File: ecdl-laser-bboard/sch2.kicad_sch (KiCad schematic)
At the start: 0 parts

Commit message: slow bias DAC
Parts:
- added C38: 0.1u, Capacitor_SMD:C_0603_1608Metric, symbol Device:C
- added C39: 1u, Capacitor_SMD:C_0603_1608Metric, symbol Device:C
- added C40: 0.22u, Capacitor_SMD:C_0603_1608Metric, symbol Device:C
- added D5: D_Zener, symbol Device:D_Zener
- added IC1: DAC80501ZDGSR, SOP50P490X110-10N, symbol DAC80501ZDGSR:DAC80501ZDGSR
- added Q1: 2N7002, Package_TO_SOT_SMD:SOT-23, symbol Transistor_FET:2N7002
- added R28: 1k, Resistor_SMD:R_0603_1608Metric, symbol Device:R
- added R29: 100k, Resistor_SMD:R_0603_1608Metric, symbol Device:R
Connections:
- new net: D5.1 (K), Q1.1 (G), R28.2, R29.1
- new net +5V: C38.1, C39.1, IC1.1 (VDD)
- new net LDTC_COM: C38.2, C39.2, C40.2, D5.2 (A), IC1.4 (AGND), Q1.2 (S), R29.2
- new net LD_SHD: Q1.3 (D)
- new net RP_EN: R28.1
- new net V_REF: C40.1, IC1.10 (VREFIO)
- no-connect marks 0 -> 2
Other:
- note added: "LD Enable"

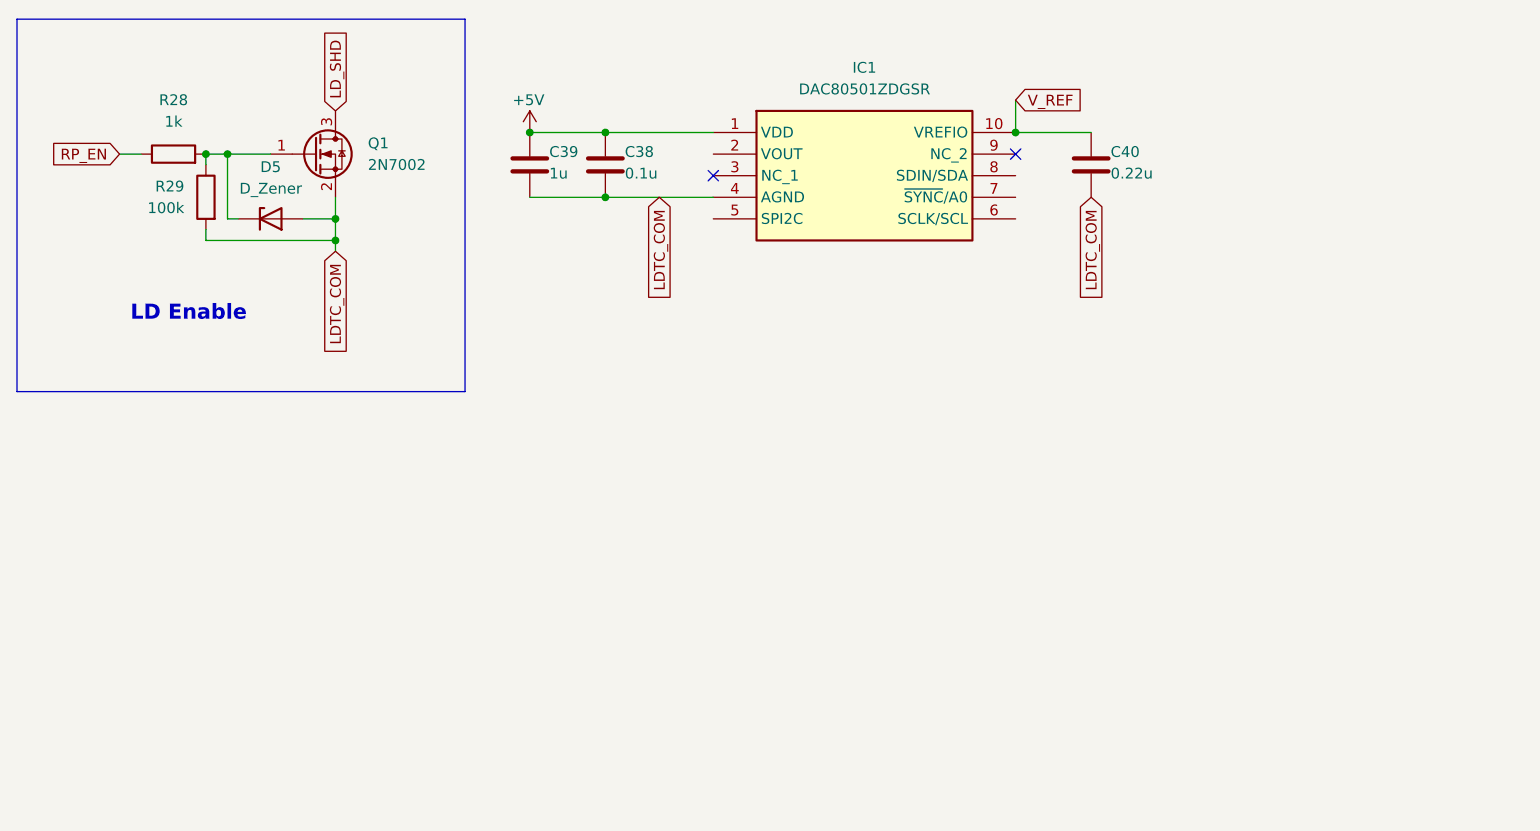
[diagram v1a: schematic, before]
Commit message: rail to rail addition
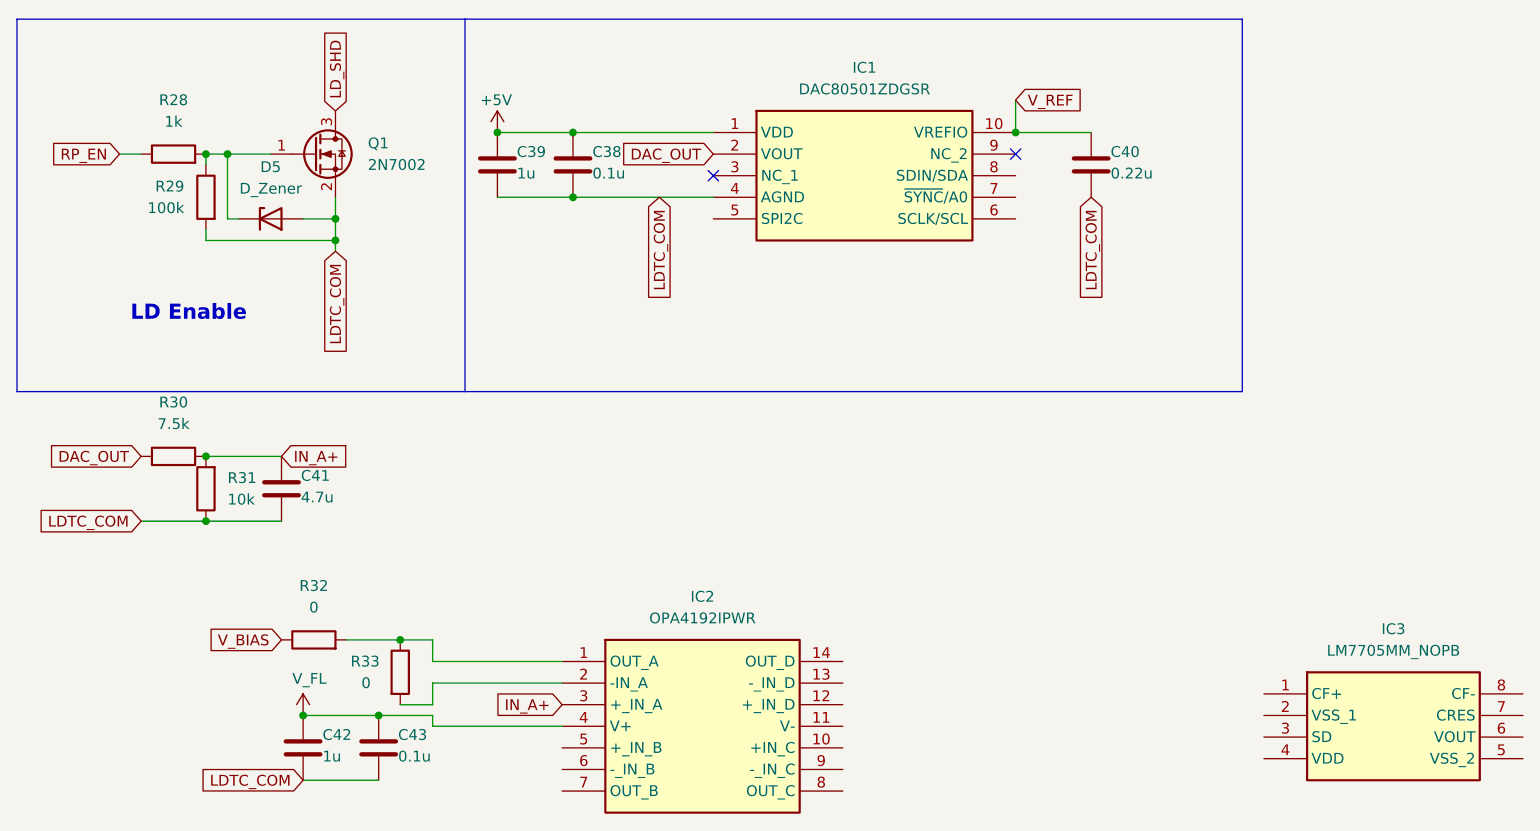
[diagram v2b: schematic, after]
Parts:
- added C41: 4.7u, Capacitor_SMD:C_0603_1608Metric, symbol Device:C
- added C42: 1u, Capacitor_SMD:C_0603_1608Metric, symbol Device:C
- added C43: 0.1u, Capacitor_SMD:C_0603_1608Metric, symbol Device:C
- added IC2: OPA4192IPWR, SOP65P640X120-14N, symbol OPA4192IPWR:OPA4192IPWR
- added IC3: LM7705MM_NOPB, SOP65P490X110-8N, symbol LM7705MM_NOPB:LM7705MM_NOPB
- added R30: 7.5k, symbol Device:R
- added R31: 10k, symbol Device:R
- added R32, R33: 0, symbol Device:R
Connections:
- net LDTC_COM: now also C41.2, C42.2, C43.2, R31.1
- net DAC_OUT: now reaches IC1.2 (VOUT)
- net DAC_OUT: now also R30.1
- new net: IC2.1 (OUT_A), R32.2, R33.1
- new net: IC2.2 (-IN_A), R33.2
- new net IN_A+: C41.1, IC2.3 (+_IN_A), R30.2, R31.2
- new net V_BIAS: R32.1
- new net V_FL: C42.1, C43.1, IC2.4 (V+)
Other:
- moved on the sheet: C38, C39

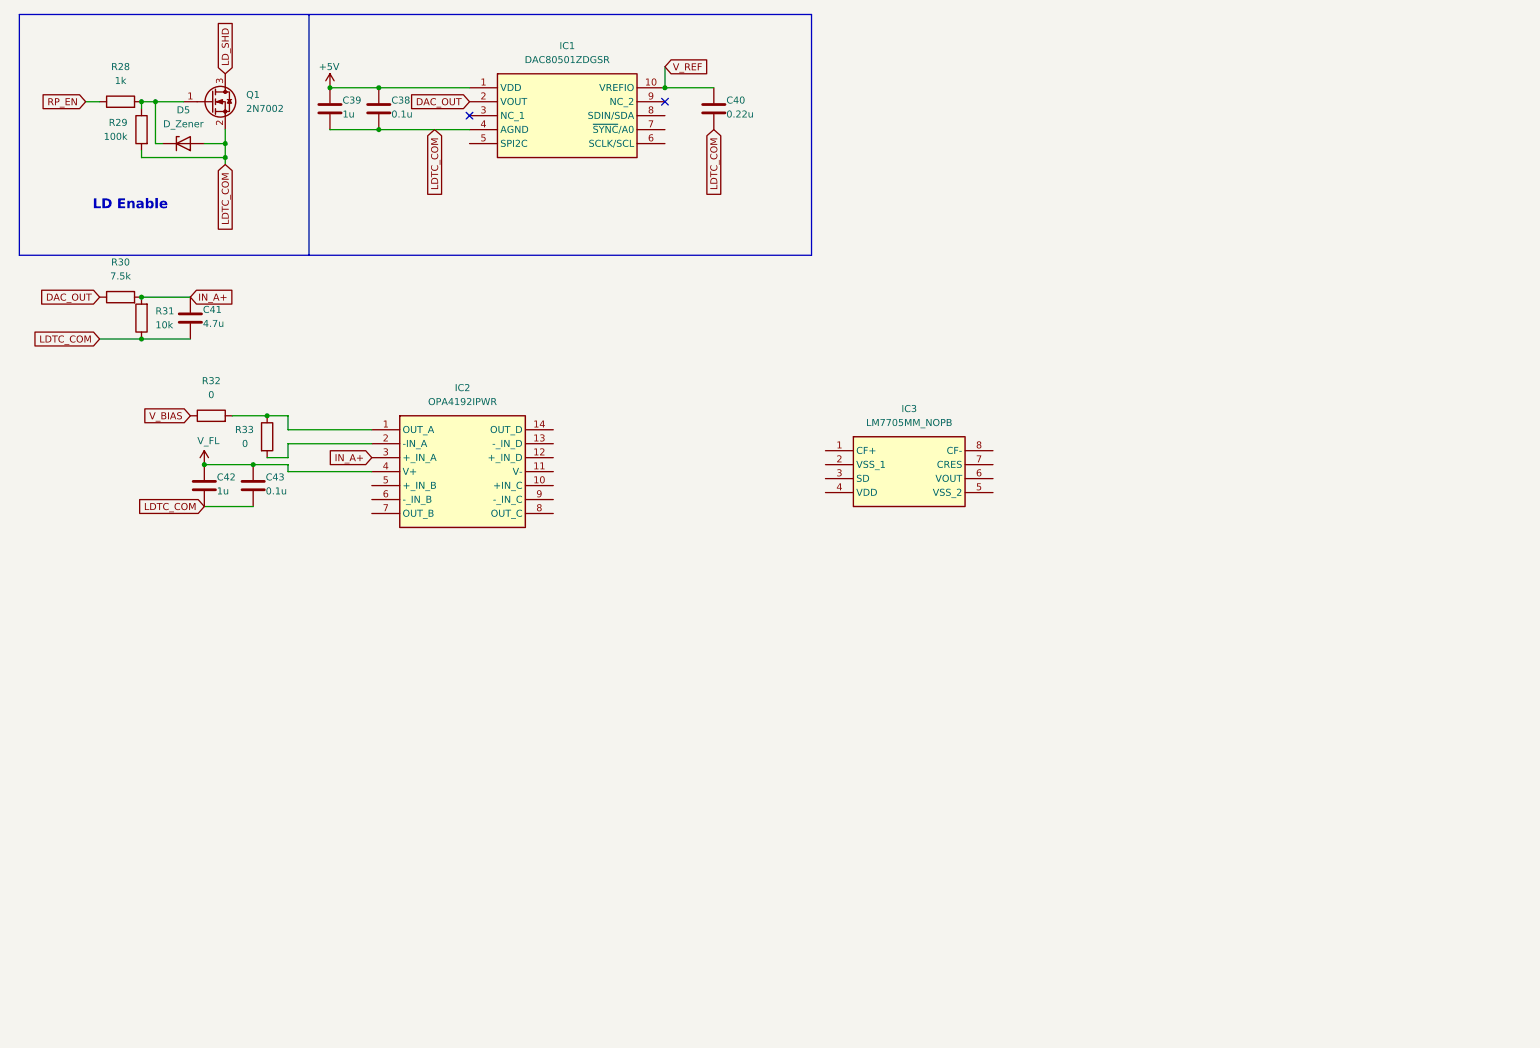
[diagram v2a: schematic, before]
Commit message: finished bias/fine tune circuit
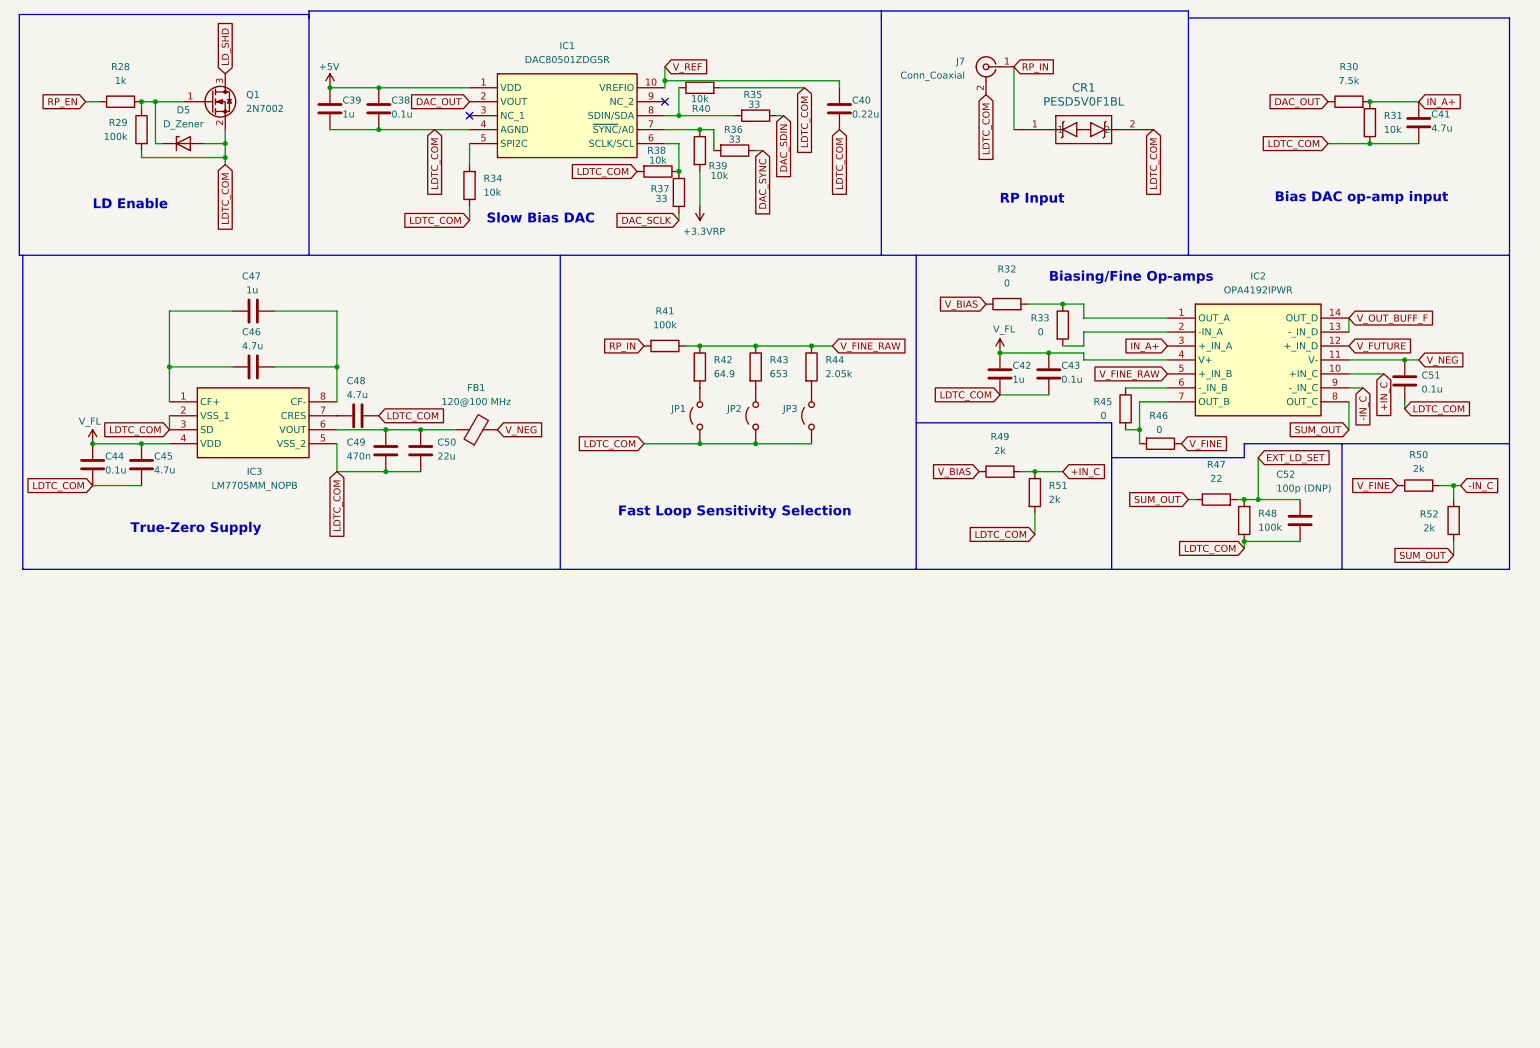
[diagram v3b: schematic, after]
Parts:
- added C44, C51: 0.1u, Capacitor_SMD:C_0603_1608Metric, symbol Device:C
- added C45, C46, C48: 4.7u, Capacitor_SMD:C_0603_1608Metric, symbol Device:C
- added C47: 1u, Capacitor_SMD:C_0603_1608Metric, symbol Device:C
- added C49: 470n, Capacitor_SMD:C_0603_1608Metric, symbol Device:C
- added C50: 22u, Capacitor_SMD:C_0603_1608Metric, symbol Device:C
- added C52: 100p (DNP), Capacitor_SMD:C_0603_1608Metric, symbol Device:C
- added CR1: PESD5V0F1BL, DFN1006-2_SOD882_NEX, symbol PESD5V0V1BL:PESD5V0F1BL
- added FB1: 120@100 MHz, symbol Device:FerriteBead
- added J7: Conn_Coaxial, symbol Connector:Conn_Coaxial
- added JP1, JP2, JP3: Jumper_2_Open, symbol Jumper:Jumper_2_Open
- added R34, R38, R39, R40: 10k, Resistor_SMD:R_0603_1608Metric, symbol Device:R
- added R35, R36, R37: 33, Resistor_SMD:R_0603_1608Metric, symbol Device:R
- added R41, R48: 100k, symbol Device:R
- added R42: 64.9, symbol Device:R
- added R43: 653, symbol Device:R
- added R44: 2.05k, symbol Device:R
- added R45, R46: 0, symbol Device:R
- added R47: 22, symbol Device:R
- added R49, R50, R51, R52: 2k, symbol Device:R
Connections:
- net LDTC_COM: now also IC3.2 (VSS_1), IC3.3 (SD), IC3.5 (VSS_2), C44.2, C45.2, C48.2, C49.1, C50.2, C51.2, C52.2, CR1.2, J7.2 (Ext), JP1.2 (B), JP2.2 (B), JP3.2 (B), R34.1, R38.2, R40.2, R48.1, R51.2
- net V_BIAS: now also R49.1
- net V_FL: now also IC3.4 (VDD), C44.1, C45.1
- net at IC3.1 (CF+): now also C46.1, C47.1
- net at IC3.6 (VOUT): now also C49.2, C50.1, FB1.1
- net at IC3.7 (CRES): now also C48.1
- net at IC3.8 (CF-): now also C46.2, C47.2
- net +IN_C: now reaches IC2.10 (+IN_C)
- net +IN_C: now also R49.2, R51.1
- net V_NEG: now reaches IC2.11 (V-)
- net V_NEG: now also C51.1, FB1.2
- net V_FUTURE: now reaches IC2.12 (+_IN_D)
- net V_OUT_BUFF_F: now reaches IC2.13 (-_IN_D)
- net V_OUT_BUFF_F: now also IC2.14 (OUT_D)
- net V_FINE_RAW: now reaches IC2.5 (+_IN_B)
- net V_FINE_RAW: now also R41.1, R42.1, R43.1, R44.1
- net at IC2.6 (-_IN_B): now also R45.1
- net at IC2.7 (OUT_B): now also R45.2, R46.2
- net SUM_OUT: now reaches IC2.8 (OUT_C)
- net SUM_OUT: now also R47.1, R52.1
- net -IN_C: now reaches IC2.9 (-_IN_C)
- net -IN_C: now also R50.2, R52.2
- net at IC1.5 (SPI2C): now also R34.2
- net at IC1.6 (SCLK/SCL): now also R37.1, R38.1
- net at IC1.7 (~{SYNC}/A0): now also R36.2, R39.1
- net at IC1.8 (SDIN/SDA): now also R35.2, R40.1
- new net: JP3.1 (A), R44.2
- new net: JP2.1 (A), R43.2
- new net: JP1.1 (A), R42.2
- new net +3.3VRP: R39.2
- new net DAC_SCLK: R37.2
- new net DAC_SDIN: R35.1
- new net DAC_SYNC: R36.1
- new net EXT_LD_SET: C52.1, R47.2, R48.2
- new net RP_IN: CR1.1, J7.1 (In), R41.2
- new net V_FINE: R46.1, R50.1
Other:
- note added: "Bias DAC op-amp input"
- note added: "Biasing/Fine Op-amps"
- note added: "Fast Loop Sensitivity Selection"
- note added: "RP Input"
- note added: "Slow Bias DAC"
- note added: "True-Zero Supply"
- moved on the sheet: C40, C41, C42, C43, IC2, IC3, R30, R31, R32, R33

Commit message: saving progress before Chipotle lol
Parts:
- added C53: 0.1u, Capacitor_SMD:C_0603_1608Metric, symbol Device:C
- added C54: 1u, Capacitor_SMD:C_0603_1608Metric, symbol Device:C
- C46: value 4.7u -> 10u
- C48: value 4.7u -> 22u
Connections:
- net IN_A+: now also C53.1
- net LDTC_COM: now also C53.2, C54.2
- net V_NEG: now also C54.1
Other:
- moved on the sheet: C41, R30, R31

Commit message: post chipotle GPIO progress
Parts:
- removed FB1: 120@100 MHz, symbol Device:FerriteBead
- added C55, C60, C63, C66: 390p, symbol Device:C
- added C56, C61, C64, C67: 0.1u, symbol Device:C
- added C59, C62, C65, C68: 10n, symbol Device:C
- added R53, R57, R58, R60, R63, R64, R66, R69, R70, R72, R75, R76: 1k, symbol Device:R
- added R54, R61, R67, R73: 1M, symbol Device:R
- added R55, R62, R68, R74: 37.4, symbol Device:R
- added R56, R59, R65, R71: 10k, symbol Device:R
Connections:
- net V_FUTURE is gone; now on net LDTC_COM: IC2.12 (+_IN_D)
- net V_OUT_BUFF_F is gone; now on net LDTC_COM: IC2.13 (-_IN_D), IC2.14 (OUT_D)
- net LDTC_COM: now also C56.2, C59.2, C61.2, C62.2, C64.2, C65.2, C67.2, C68.2, R54.1, R61.1, R67.1, R73.1
- net V_NEG: now also C49.2, C50.1, IC3.6 (VOUT)
- new net: C66.2, R71.2
- new net: C55.2, R56.2
- new net: C63.2, R65.2
- new net: C60.2, R59.2
- new net ACT_T_MON: R72.1
- new net ACT_T_MON_+: R72.2, R73.2
- new net ACT_T_MON_-: R71.1, R75.1
- new net ACT_T_MON_out: C66.1, R74.1
- new net AIN0: C59.1, R58.2
- new net AIN1: C62.1, R64.2
- new net AIN2: C65.1, R70.2
- new net AIN3: C68.1, R76.2
- new net LD_I_MON: R53.1
- new net LD_I_MON_+: R53.2, R54.2
- new net LD_I_MON_-: R56.1, R57.1
- new net LD_I_MON_out: C55.1, R55.1
- new net LD_P_MON: R60.1
- new net LD_P_MON_+: R60.2, R61.2
- new net LD_P_MON_-: R59.1, R63.1
- new net LD_P_MON_out: C60.1, R62.1
- new net SET_T_MON: R66.1
- new net SET_T_MON_+: R66.2, R67.2
- new net SET_T_MON_-: R65.1, R69.1
- new net SET_T_MON_out: C63.1, R68.1
- new net V_ACT_T_MON_OUT: C67.1, R74.2, R75.2, R76.1
- new net V_LDI_MON_OUT: C56.1, R55.2, R57.2, R58.1
- new net V_LDP_MON_OUT: C61.1, R62.2, R63.2, R64.1
- new net V_SET_T_MON_OUT: C64.1, R68.2, R69.2, R70.1
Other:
- note added: "ACT T MON"
- note added: "LD I Mon"
- note added: "LD P Mon"
- note added: "SET T MON"

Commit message: begun layout
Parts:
- removed JP1, JP2, JP3: Jumper_2_Open, symbol Jumper:Jumper_2_Open
- added J13: M20-9980346, M20-9980346:HDRV6W64P254_2X3_762X508X864P, symbol M20-9980346:M20-9980346
- added TP10: LD SHD, TestPoint:TestPoint_Keystone_5015_Micro_Mini, symbol Connector:TestPoint
- added TP4: V_NEG, TestPoint:TestPoint_Keystone_5015_Micro_Mini, symbol Connector:TestPoint
- added TP5: V_FINE, TestPoint:TestPoint_Keystone_5015_Micro_Mini, symbol Connector:TestPoint
- added TP6: V_FINE_RAW, TestPoint:TestPoint_Keystone_5015_Micro_Mini, symbol Connector:TestPoint
- added TP7: V_BIAS, TestPoint:TestPoint_Keystone_5015_Micro_Mini, symbol Connector:TestPoint
- added TP8: SUM_OUT, TestPoint:TestPoint_Keystone_5015_Micro_Mini, symbol Connector:TestPoint
- added TP9: EXT LD, TestPoint:TestPoint_Keystone_5015_Micro_Mini, symbol Connector:TestPoint
- C50: footprint Capacitor_SMD:C_0603_1608Metric -> Capacitor_SMD:C_1210_3225Metric
- C55, C59, C60, C62, C63, C65, C66, C68: footprint (none) -> Capacitor_SMD:C_0402_1005Metric
- C56, C61, C64, C67: footprint (none) -> Capacitor_SMD:C_0603_1608Metric
- CR1: footprint DFN1006-2_SOD882_NEX -> PESD5V0F1BL:DFN1006-2_SOD882_NEX
- D5: footprint (none) -> Diode_SMD:D_SOD-323F
- IC1: footprint SOP50P490X110-10N -> DAC80501:SOP50P490X110-10N
- IC2: footprint SOP65P640X120-14N -> OPA4192:SOP65P640X120-14N
- IC3: footprint SOP65P490X110-8N -> LM7705MM:SOP65P490X110-8N
- J7: footprint (none) -> SMA-J-P-H-ST-TH1:CONN_SMA-J-P-H-ST-TH1_SAI
- R30, R31, R41, R44, R47, R48, R49, R50, R51, R52, R53, R54, R55, R56, R57, R58, R59, R60, R61, R62, R63, R64, R65, R66, R67, R68, R69, R70, R71, R72, R73, R74, R75, R76: footprint (none) -> Resistor_SMD:R_0603_1608Metric
- R32, R33, R45, R46: footprint (none) -> Resistor_SMD:R_0805_2012Metric
- R42: value 64.9 -> 67; footprint (none) -> Resistor_SMD:R_0603_1608Metric
- R43: value 653 -> 953; footprint (none) -> Resistor_SMD:R_0603_1608Metric
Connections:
- net +5V is gone; now on net V_FL: C38.1, C39.1, IC1.1 (VDD)
- net EXT_LD_SET: now also TP9.1
- net LDTC_COM: now also R44.2, J13.2, J13.4
- net LD_SHD: now also TP10.1
- net SUM_OUT: now also TP8.1
- net V_BIAS: now also TP7.1
- net V_FINE: now also TP5.1
- net V_FINE_RAW: now also TP6.1
- net V_NEG: now also TP4.1
- net at R43.2: now also J13.3
- net at R42.2: now also J13.1
- no-connect marks 2 -> 4
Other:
- moved on the sheet: R41, R42, R43, R44

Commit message: layout v0
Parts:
- R30: value 7.5k -> 63.4k
- R35, R36, R37: value 33 -> 1k
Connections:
- net LDTC_COM: no longer IC2.13 (-_IN_D), IC2.14 (OUT_D)
- new net: IC2.13 (-_IN_D), IC2.14 (OUT_D)
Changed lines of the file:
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@@
 	)
 	(junction
-		(at 254 69.85)
-		(diameter 0)
-		(color 0 0 0 0)
-	)
-	(junction
 		(at 135.89 67.31)
 		(diameter 0)
@@
 	(wire
 		(pts
+			(xy 254 67.31) (xy 254 69.85)
+		)
+		(stroke
+			(width 0)
+			(type default)
+		)
+	)
+	(wire
+		(pts
 			(xy 246.38 139.7) (xy 243.84 139.7)
 		)
@@
 	(wire
 		(pts
-			(xy 254 69.85) (xy 254 72.39)
-		)
-		(stroke
-			(width 0)
-			(type default)
-		)
-	)
-	(wire
-		(pts
 			(xy 78.74 87.63) (xy 85.09 87.63)
 		)
@@
 	(wire
 		(pts
-			(xy 254 67.31) (xy 254 69.85)
-		)
-		(stroke
-			(width 0)
-			(type default)
-		)
-	)
-	(wire
-		(pts
 			(xy 166.37 152.4) (xy 175.26 152.4)
 		)
@@
 	(global_label "LDTC_COM"
 		(shape input)
-		(at 254 69.85 0)
+		(at 254 72.39 0)
 		(fields_autoplaced yes)
 		(effects
@@
 		)
 		(property "Intersheetrefs" "${INTERSHEET_REFS}"
-			(at 266.5404 69.85 0)
+			(at 266.5404 72.39 0)
 			(hide yes)
 			(show_name no)
@@
 			)
 		)
-		(property "Value" "33"
+		(property "Value" "1k"
 			(at 128.905 45.593 0)
 			(show_name no)
@@
 			)
 		)
-		(property "Value" "33"
+		(property "Value" "1k"
 			(at 142.24 34.798 90)
 			(show_name no)
@@
 			)
 		)
-		(property "Value" "7.5k"
+		(property "Value" "63.4k"
 			(at 245.11 24.13 90)
 			(show_name no)
@@
 			)
 		)
-		(property "Value" "33"
+		(property "Value" "1k"
 			(at 145.796 28.448 90)
 			(show_name no)
